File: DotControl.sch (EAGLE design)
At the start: 24 parts, among them CN1 1X4-BIG, J3 USB-MICROB, SW2 Previous, SW5 Previous, SW6 Next, SW8 Ok, U1 ATMEGA328P-MU-QFN32

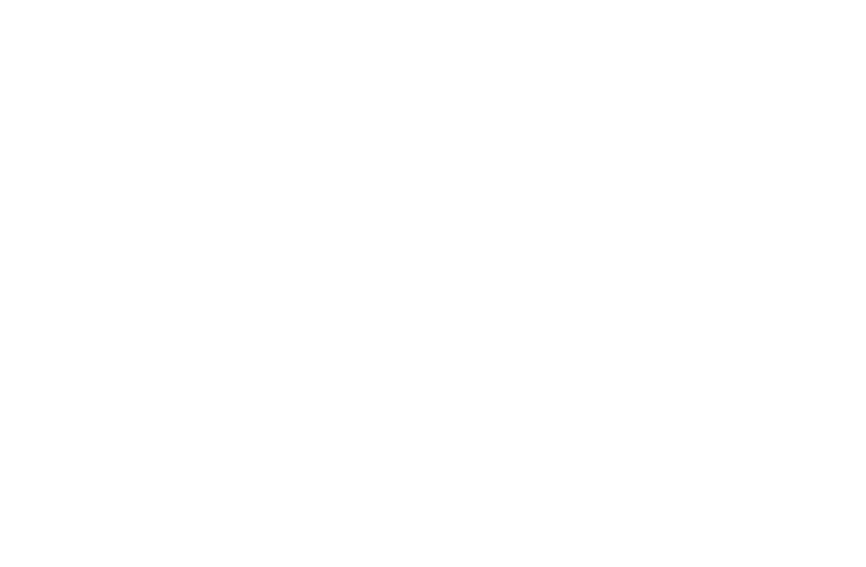
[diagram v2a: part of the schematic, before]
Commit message: Add TMP112 temperature sensor
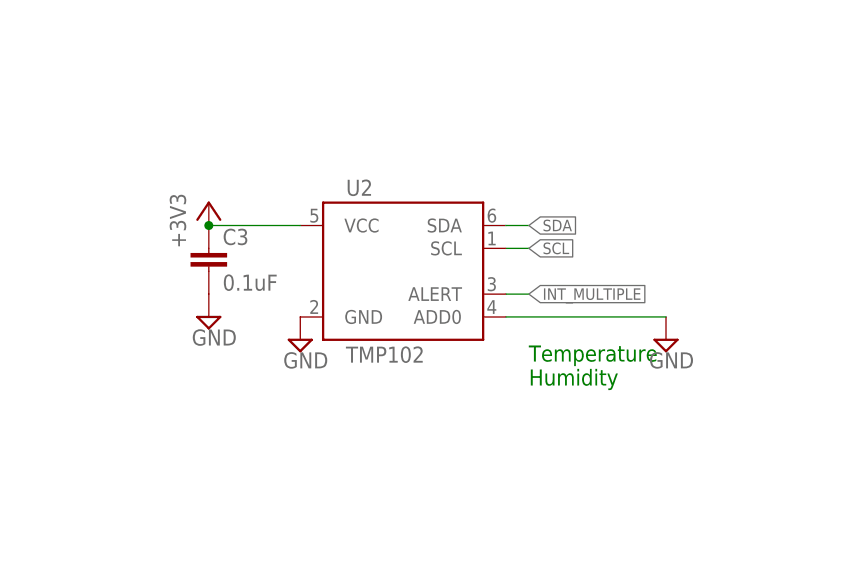
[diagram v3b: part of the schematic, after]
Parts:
- added C3: 0.1uF, resistor:C-EUC0603
- added U2: TMP102, SparkFun:TMP102
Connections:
- new net INT_MULTIPLE: U2.ALERT
- net +3V3: now also C3.1, U2.VCC
- net GND: now also C3.2, U2.ADD0, U2.GND
- net SCL: now also U2.SCL
- net SDA: now also U2.SDA
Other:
- note added: "Temperature Humidity"
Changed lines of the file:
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@@
 <setting verticaltext="up"/>
 </settings>
-<grid distance="0.05" unitdist="inch" unit="inch" style="lines" multiple="1" display="no" altdistance="0.01" altunitdist="inch" altunit="inch"/>
+<grid distance="0.1" unitdist="inch" unit="inch" style="lines" multiple="1" display="no" altdistance="0.01" altunitdist="inch" altunit="inch"/>
 <layers>
 <layer number="1" name="Top" color="4" fill="1" visible="no" active="no"/>
@@
 <part name="P+2" library="supply1" deviceset="+5V" device=""/>
 <part name="P+5" library="supply1" deviceset="+5V" device=""/>
+<part name="U2" library="SparkFun" deviceset="TMP102" device=""/>
+<part name="SUPPLY15" library="supply2" deviceset="GND" device=""/>
+<part name="+3V11" library="supply1" deviceset="+3V3" device=""/>
+<part name="C3" library="resistor" deviceset="C-EU" device="C0603" value="0.1uF"/>
+<part name="SUPPLY12" library="supply2" deviceset="GND" device=""/>
+<part name="SUPPLY7" library="supply2" deviceset="GND" device=""/>
 </parts>
 <sheets>
@@
 <text x="223.52" y="177.8" size="1.778" layer="91">Do not put 3V3 when battery on!</text>
 <text x="81.28" y="96.52" size="1.27" layer="91">Always enable internal pullup beforehand!</text>
+<text x="238.76" y="91.44" size="1.778" layer="91">Temperature
+Humidity</text>
 </plain>
 <instances>
@@
 <instance part="P+2" gate="1" x="52.07" y="147.32"/>
 <instance part="P+5" gate="1" x="148.59" y="161.29"/>
+<instance part="U2" gate="G$1" x="226.06" y="104.14"/>
+<instance part="SUPPLY15" gate="GND" x="213.36" y="96.52"/>
+<instance part="+3V11" gate="G$1" x="203.2" y="111.76"/>
+<instance part="C3" gate="G$1" x="203.2" y="106.68"/>
+<instance part="SUPPLY12" gate="GND" x="203.2" y="99.06"/>
+<instance part="SUPPLY7" gate="GND" x="254" y="96.52"/>
 </instances>
 <busses>
@@
 <pinref part="SUPPLY5" gate="GND" pin="GND"/>
 </segment>
+<segment>
+<pinref part="U2" gate="G$1" pin="GND"/>
+<pinref part="SUPPLY15" gate="GND" pin="GND"/>
+</segment>
+<segment>
+<pinref part="C3" gate="G$1" pin="2"/>
+<pinref part="SUPPLY12" gate="GND" pin="GND"/>
+</segment>
+<segment>
+<pinref part="U2" gate="G$1" pin="ADD0"/>
+<wire x1="236.22" y1="99.06" x2="254" y2="99.06" width="0.1524" layer="91"/>
+<pinref part="SUPPLY7" gate="GND" pin="GND"/>
+</segment>
 </net>
 <net name="SCK" class="0">
@@
 <label x="59.69" y="195.58" size="1.27" layer="95" rot="R180" xref="yes"/>
 </segment>
+<segment>
+<pinref part="U2" gate="G$1" pin="SDA"/>
+<wire x1="236.22" y1="109.22" x2="238.76" y2="109.22" width="0.1524" layer="91"/>
+<label x="238.76" y="109.22" size="1.27" layer="95" xref="yes"/>
+</segment>
 </net>
 <net name="SCL" class="0">
@@
 <wire x1="63.5" y1="200.66" x2="59.69" y2="200.66" width="0.1524" layer="91"/>
 <label x="59.69" y="200.66" size="1.27" layer="95" rot="R180" xref="yes"/>
+</segment>
+<segment>
+<pinref part="U2" gate="G$1" pin="SCL"/>
+<wire x1="236.22" y1="106.68" x2="238.76" y2="106.68" width="0.1524" layer="91"/>
+<label x="238.76" y="106.68" size="1.27" layer="95" xref="yes"/>
 </segment>
 </net>
@@
 <pinref part="+3V7" gate="G$1" pin="+3V3"/>
 </segment>
+<segment>
+<pinref part="+3V11" gate="G$1" pin="+3V3"/>
+<pinref part="C3" gate="G$1" pin="1"/>
+<wire x1="203.2" y1="109.22" x2="213.36" y2="109.22" width="0.1524" layer="91"/>
+<junction x="203.2" y="109.22"/>
+<pinref part="U2" gate="G$1" pin="VCC"/>
+</segment>
 </net>
 <net name="PUSH" class="0">
@@
 </segment>
 </net>
+<net name="INT_MULTIPLE" class="0">
+<segment>
+<pinref part="U2" gate="G$1" pin="ALERT"/>
+<wire x1="236.22" y1="101.6" x2="238.76" y2="101.6" width="0.1524" layer="91"/>
+<label x="238.76" y="101.6" size="1.27" layer="95" xref="yes"/>
+</segment>
+</net>

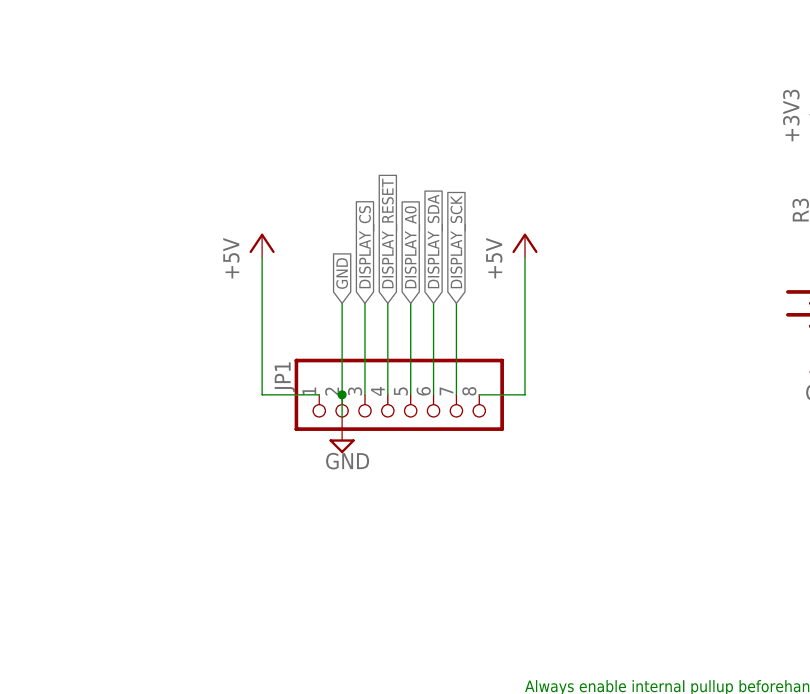
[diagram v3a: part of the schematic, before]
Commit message: Add connections for 128x128
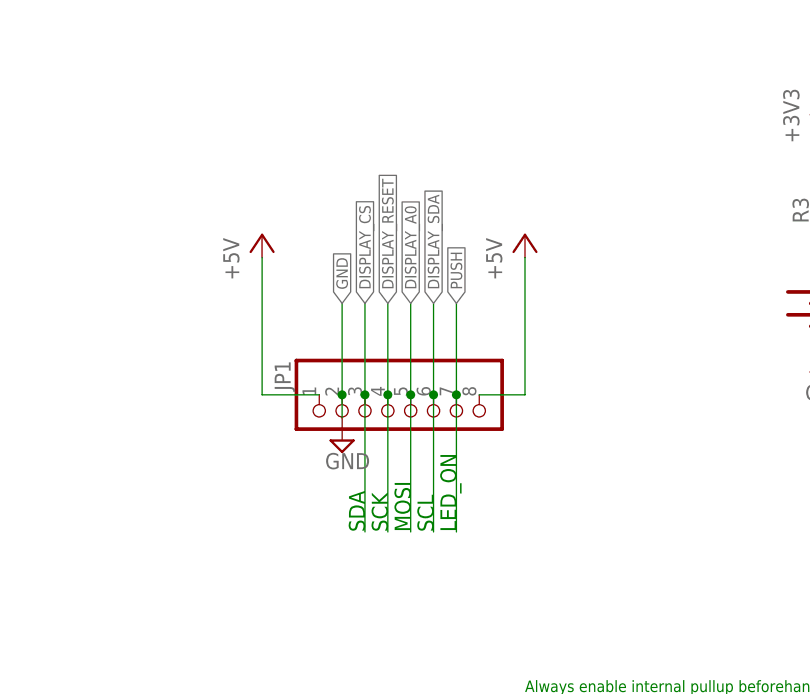
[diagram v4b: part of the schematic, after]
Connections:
- removed net DISPLAY_SCK: JP1.7
- net PUSH: now also JP1.7
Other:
- note added: "LED_ON"
- note added: "MOSI"
- note added: "SCK"
- note added: "SCL"
- note added: "SDA"
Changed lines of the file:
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@@
 <text x="238.76" y="91.44" size="1.778" layer="91">Temperature
 Humidity</text>
+<text x="68.58" y="114.3" size="1.778" layer="91" rot="R90">MOSI</text>
+<text x="66.04" y="114.3" size="1.778" layer="91" rot="R90">SCK</text>
+<text x="63.5" y="114.3" size="1.778" layer="91" rot="R90">SDA</text>
+<text x="71.12" y="114.3" size="1.778" layer="91" rot="R90">SCL</text>
+<text x="73.66" y="114.3" size="1.778" layer="91" rot="R90">LED_ON</text>
 </plain>
 <instances>
@@
 <label x="68.58" y="139.7" size="1.27" layer="95" rot="R90" xref="yes"/>
 <pinref part="JP1" gate="G$1" pin="5"/>
+<wire x1="68.58" y1="129.54" x2="68.58" y2="114.3" width="0.1524" layer="91"/>
+<junction x="68.58" y="129.54"/>
 </segment>
 </net>
@@
 <label x="66.04" y="139.7" size="1.27" layer="95" rot="R90" xref="yes"/>
 <pinref part="JP1" gate="G$1" pin="4"/>
+<wire x1="66.04" y1="129.54" x2="66.04" y2="114.3" width="0.1524" layer="91"/>
+<junction x="66.04" y="129.54"/>
 </segment>
 </net>
@@
 <label x="63.5" y="139.7" size="1.27" layer="95" rot="R90" xref="yes"/>
 <pinref part="JP1" gate="G$1" pin="3"/>
+<wire x1="63.5" y1="129.54" x2="63.5" y2="114.3" width="0.1524" layer="91"/>
+<junction x="63.5" y="129.54"/>
 </segment>
 </net>
@@
 <label x="71.12" y="139.7" size="1.27" layer="95" rot="R90" xref="yes"/>
 <pinref part="JP1" gate="G$1" pin="6"/>
-</segment>
-</net>
-<net name="DISPLAY_SCK" class="0">
-<segment>
-<wire x1="73.66" y1="129.54" x2="73.66" y2="139.7" width="0.1524" layer="91"/>
-<label x="73.66" y="139.7" size="1.27" layer="95" rot="R90" xref="yes"/>
-<pinref part="JP1" gate="G$1" pin="7"/>
+<wire x1="71.12" y1="129.54" x2="71.12" y2="114.3" width="0.1524" layer="91"/>
+<junction x="71.12" y="129.54"/>
 </segment>
 </net>
@@
 <label x="330.2" y="185.42" size="1.27" layer="95" xref="yes"/>
 </segment>
-</net>
+<segment>
+<wire x1="73.66" y1="129.54" x2="73.66" y2="139.7" width="0.1524" layer="91"/>
+<label x="73.66" y="139.7" size="1.27" layer="95" rot="R90" xref="yes"/>
+<pinref part="JP1" gate="G$1" pin="7"/>
+<wire x1="73.66" y1="129.54" x2="73.66" y2="114.3" width="0.1524" layer="91"/>
+<junction x="73.66" y="129.54"/>
+</segment>
+</net>
